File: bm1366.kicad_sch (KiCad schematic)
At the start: 7 parts, among them J2 Conn_01x06, U35 TXU0304PW, U8 25MHz

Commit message: Added 4th Phase Buck
Started to add 4th Phase for the Buck, implementing BM1370 footprint etc
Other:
- sheet BM1368 renamed BM1370
- sheet BM1368-1 renamed BM1370-1
- sheet BM1368-2 renamed BM1370-2
- sheet BM1368-3 renamed BM1370-3
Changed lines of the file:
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@@
 			(color 255 255 194 1.0000)
 		)
-		(property "Sheetname" "BM1368"
+		(property "Sheetname" "BM1370"
 			(at 83.82 65.3284 0)
 			(effects
@@
 			(color 255 255 194 1.0000)
 		)
-		(property "Sheetname" "BM1368-1"
+		(property "Sheetname" "BM1370-1"
 			(at 124.46 65.3284 0)
 			(effects
@@
 			(color 255 255 194 1.0000)
 		)
-		(property "Sheetname" "BM1368-3"
+		(property "Sheetname" "BM1370-3"
 			(at 199.39 65.3284 0)
 			(effects
@@
 			(color 255 255 194 1.0000)
 		)
-		(property "Sheetname" "BM1368-2"
+		(property "Sheetname" "BM1370-2"
 			(at 162.56 65.3284 0)
 			(effects

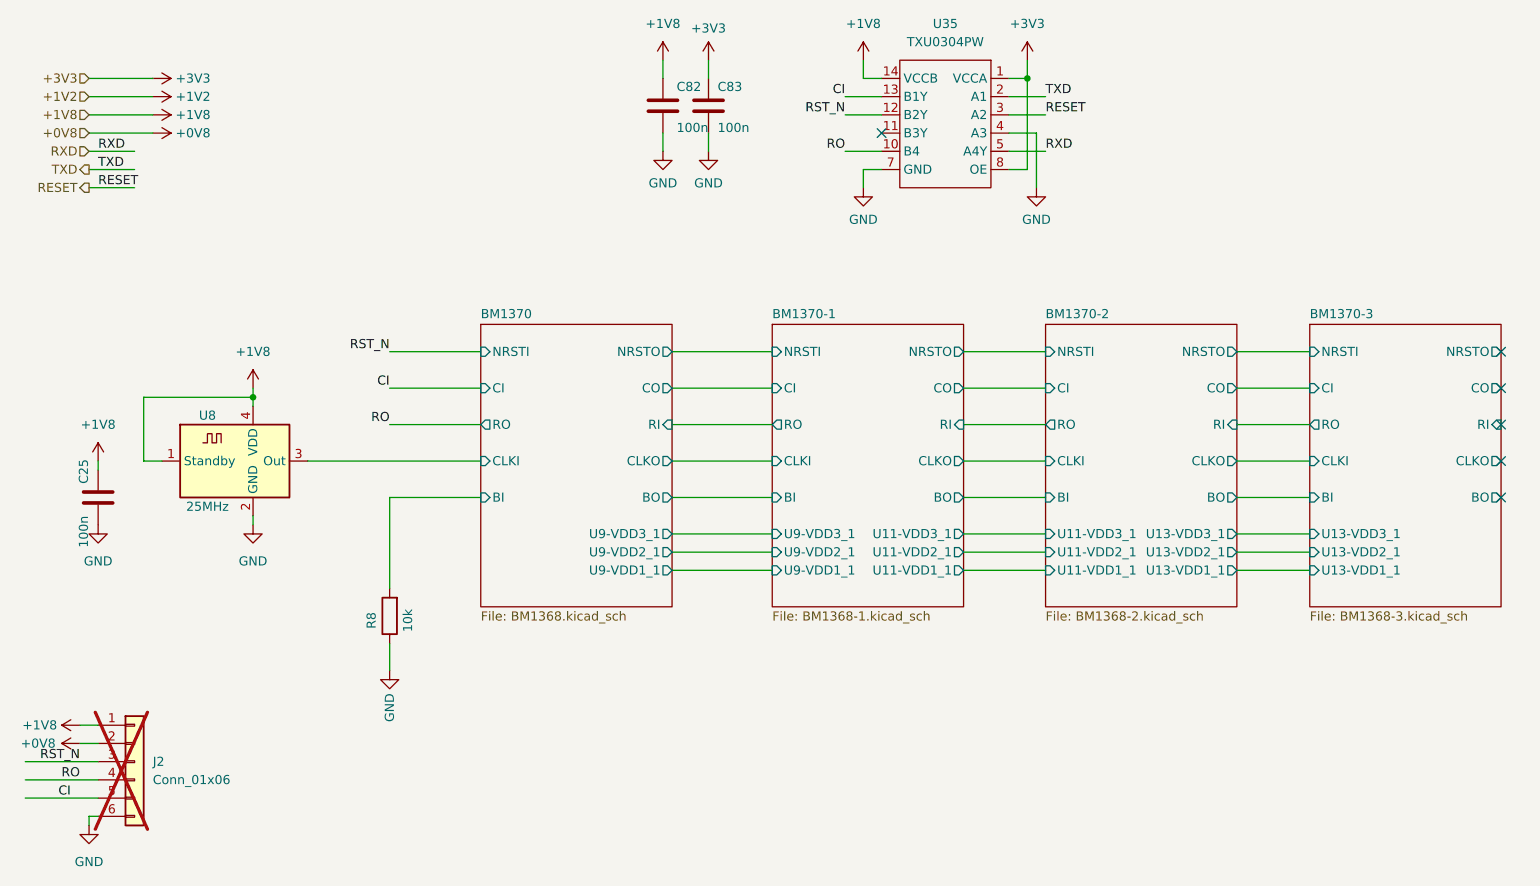
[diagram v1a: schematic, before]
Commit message: Changed LDO to 1V2 and original 1V2 to VDD
1V8 LDO replaced with 1V2 LDO
Crystal replaced
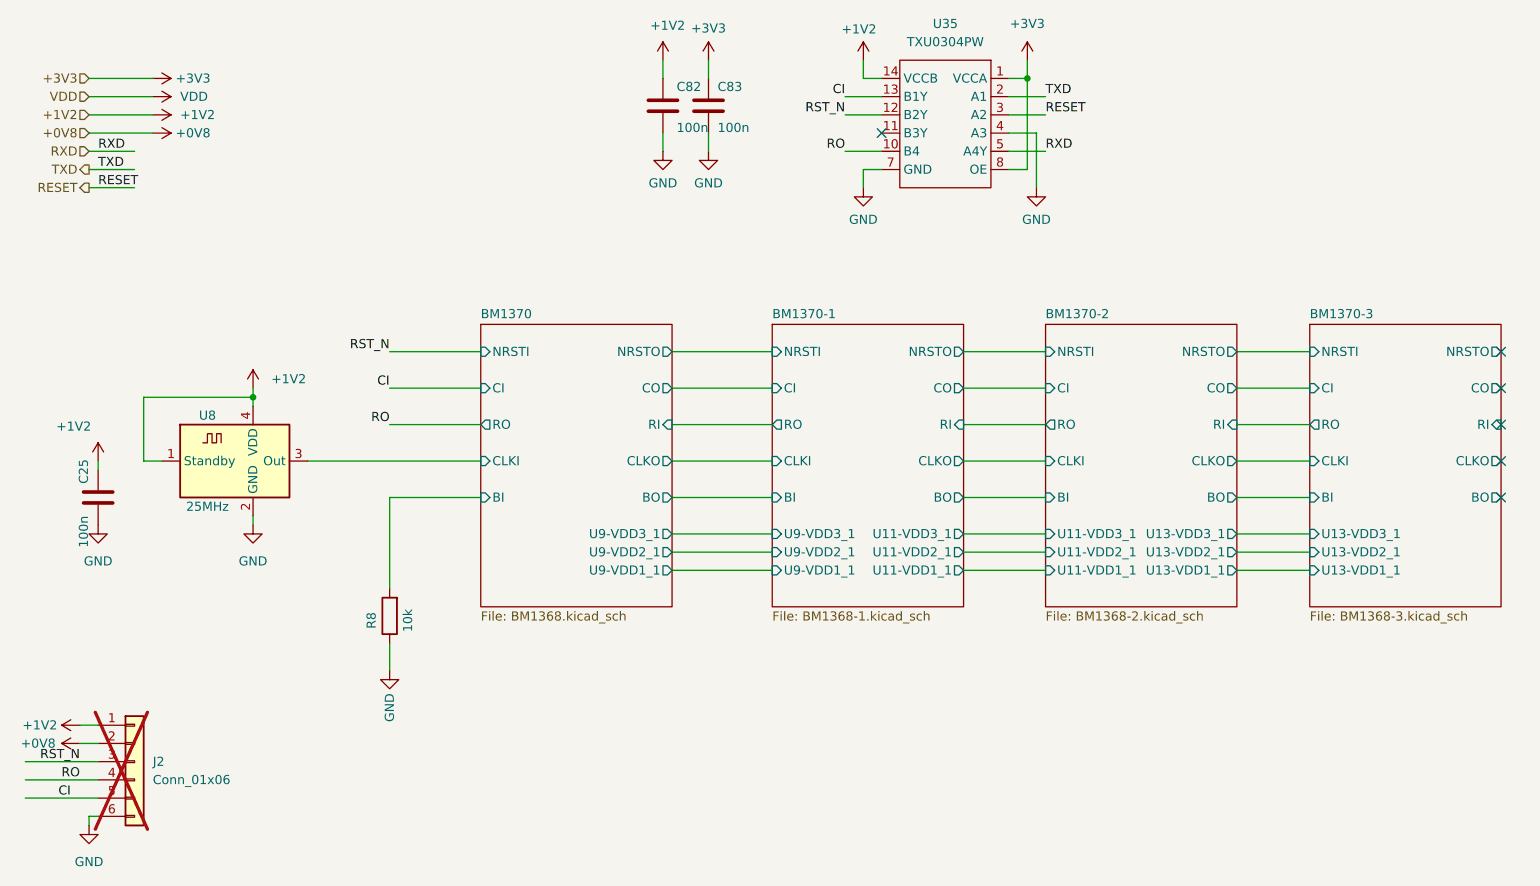
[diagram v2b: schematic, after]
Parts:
- U8: Distributor (none) -> D; OrderNr (none) -> 1923-1664-1-ND
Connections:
- net +1V8 is gone; now on net +1V2: C25.1, C82.1, J2.1 (Pin_1), U35.14 (VCCB), U8.1 (Standby), U8.4 (VDD)
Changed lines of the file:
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@@
 		)
 	)
-	(hierarchical_label "+1V8"
+	(hierarchical_label "+1V2"
 		(shape input)
 		(at 29.21 36.83 180)
@@
 		)
 	)
-	(hierarchical_label "+1V2"
+	(hierarchical_label "VDD"
 		(shape input)
 		(at 29.21 34.29 180)
@@
 	)
 	(symbol
-		(lib_id "power:+1V2")
+		(lib_id "power:VDD")
 		(at 38.1 34.29 270)
 		(unit 1)
@@
 			)
 		)
-		(property "Value" "+1V2"
-			(at 41.275 34.29 90)
+		(property "Value" "VDD"
+			(at 41.91 34.2899 90)
 			(effects
 				(font
@@
 			)
 		)
-		(property "Description" ""
+		(property "Description" "Power symbol creates a global label with name \"VDD\""
 			(at 38.1 34.29 0)
 			(effects
@@
 	)
 	(symbol
-		(lib_id "power:+1V8")
+		(lib_id "power:+1V2")
 		(at 52.07 74.93 0)
 		(unit 1)
@@
 			)
 		)
-		(property "Value" "+1V8"
-			(at 52.07 69.85 0)
-			(effects
-				(font
-					(size 1.27 1.27)
-				)
+		(property "Value" "+1V2"
+			(at 54.61 73.6599 0)
+			(effects
+				(font
+					(size 1.27 1.27)
+				)
+				(justify left)
 			)
 		)
@@
 			)
 		)
-		(property "Description" ""
+		(property "Description" "Power symbol creates a global label with name \"+1V2\""
 			(at 52.07 74.93 0)
 			(effects
@@
 	)
 	(symbol
-		(lib_id "power:+1V8")
+		(lib_id "power:+1V2")
 		(at 109.22 29.21 0)
 		(unit 1)
@@
 		(on_board yes)
 		(dnp no)
-		(fields_autoplaced yes)
 		(property "Reference" "#PWR0149"
 			(at 109.22 33.02 0)
@@
 			)
 		)
-		(property "Value" "+1V8"
-			(at 109.22 24.13 0)
-			(effects
-				(font
-					(size 1.27 1.27)
-				)
+		(property "Value" "+1V2"
+			(at 107.442 24.384 0)
+			(effects
+				(font
+					(size 1.27 1.27)
+				)
+				(justify left)
 			)
 		)
@@
 			)
 		)
-		(property "Description" ""
+		(property "Description" "Power symbol creates a global label with name \"+1V2\""
 			(at 109.22 29.21 0)
 			(effects
@@
 	)
 	(symbol
-		(lib_id "power:+1V8")
+		(lib_id "power:+1V2")
 		(at 27.94 121.92 90)
 		(unit 1)
@@
 			)
 		)
-		(property "Value" "+1V8"
-			(at 24.765 121.92 90)
-			(effects
-				(font
-					(size 1.27 1.27)
-				)
-				(justify left)
+		(property "Value" "+1V2"
+			(at 22.352 121.92 90)
+			(effects
+				(font
+					(size 1.27 1.27)
+				)
 			)
 		)
@@
 			)
 		)
-		(property "Description" ""
+		(property "Description" "Power symbol creates a global label with name \"+1V2\""
 			(at 27.94 121.92 0)
 			(effects
@@
 	)
 	(symbol
-		(lib_id "power:+1V8")
+		(lib_id "power:+1V2")
 		(at 38.1 36.83 270)
 		(unit 1)
@@
 			)
 		)
-		(property "Value" "+1V8"
-			(at 41.275 36.83 90)
+		(property "Value" "+1V2"
+			(at 41.91 36.8299 90)
 			(effects
 				(font
@@
 			)
 		)
-		(property "Description" ""
+		(property "Description" "Power symbol creates a global label with name \"+1V2\""
 			(at 38.1 36.83 0)
 			(effects
@@
 	)
 	(symbol
-		(lib_id "power:+1V8")
+		(lib_id "power:+1V2")
 		(at 137.16 29.21 0)
 		(unit 1)
@@
 		(on_board yes)
 		(dnp no)
-		(fields_autoplaced yes)
 		(property "Reference" "#PWR0163"
 			(at 137.16 33.02 0)
@@
 			)
 		)
-		(property "Value" "+1V8"
-			(at 137.16 24.13 0)
-			(effects
-				(font
-					(size 1.27 1.27)
-				)
+		(property "Value" "+1V2"
+			(at 134.112 24.892 0)
+			(effects
+				(font
+					(size 1.27 1.27)
+				)
+				(justify left)
 			)
 		)
@@
 			)
 		)
-		(property "Description" ""
+		(property "Description" "Power symbol creates a global label with name \"+1V2\""
 			(at 137.16 29.21 0)
 			(effects
@@
 	)
 	(symbol
-		(lib_id "power:+1V8")
+		(lib_id "power:+1V2")
 		(at 30.48 85.09 0)
 		(unit 1)
@@
 		(on_board yes)
 		(dnp no)
-		(fields_autoplaced yes)
 		(property "Reference" "#PWR054"
 			(at 30.48 88.9 0)
@@
 			)
 		)
-		(property "Value" "+1V8"
-			(at 30.48 80.01 0)
-			(effects
-				(font
-					(size 1.27 1.27)
-				)
+		(property "Value" "+1V2"
+			(at 24.638 80.264 0)
+			(effects
+				(font
+					(size 1.27 1.27)
+				)
+				(justify left)
 			)
 		)
@@
 			)
 		)
-		(property "Description" ""
+		(property "Description" "Power symbol creates a global label with name \"+1V2\""
 			(at 30.48 85.09 0)
 			(effects
@@
 			)
 		)
-		(property "Datasheet" "https://abracon.com/Oscillators/ASDMB.pdf"
+		(property "Datasheet" "https://portal.iqdfrequencyproducts.com/products/pn/LFSPXO076024Reel.pdf"
 			(at 57.15 73.66 0)
 			(effects
@@
 			(at 49.53 85.09 0)
 			(effects
+				(font
+					(size 1.27 1.27)
+				)
+				(hide yes)
+			)
+		)
+		(property "OrderNr" "1923-1664-1-ND"
+			(at 49.53 85.09 0)
+			(effects
+				(font
+					(size 1.27 1.27)
+				)
+				(hide yes)
+			)
+		)
+		(property "Distributor" "D"
+			(at 49.53 85.09 0)
+			(effects

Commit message: BOM specifications
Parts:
- C25, C82, C83: value 100n -> 100n/0.7mm; Brand (none) -> YAGEO; Distributor (none) -> D; Manufacturer (none) -> AC0805KRX7R9BB104; OrderNr (none) -> 311-3037-1-ND; Size (none) -> 0805
- R8: Brand (none) -> Stackpole Electronics Inc; Distributor (none) -> D; Manufacturer (none) -> RMCF0805FT10K0; OrderNr (none) -> RMCF0805FT10K0CT-ND; Size (none) -> 0805
- U35: Brand (none) -> Texas Instruments
- U8: Brand (none) -> IQD Frequency Products; Manufacturer (none) -> LFSPXO076024
